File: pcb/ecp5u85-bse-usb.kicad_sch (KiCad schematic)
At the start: 16 parts, among them J1 BSE-040-01-X-D-A, J2 BSE-040-01-X-D-A

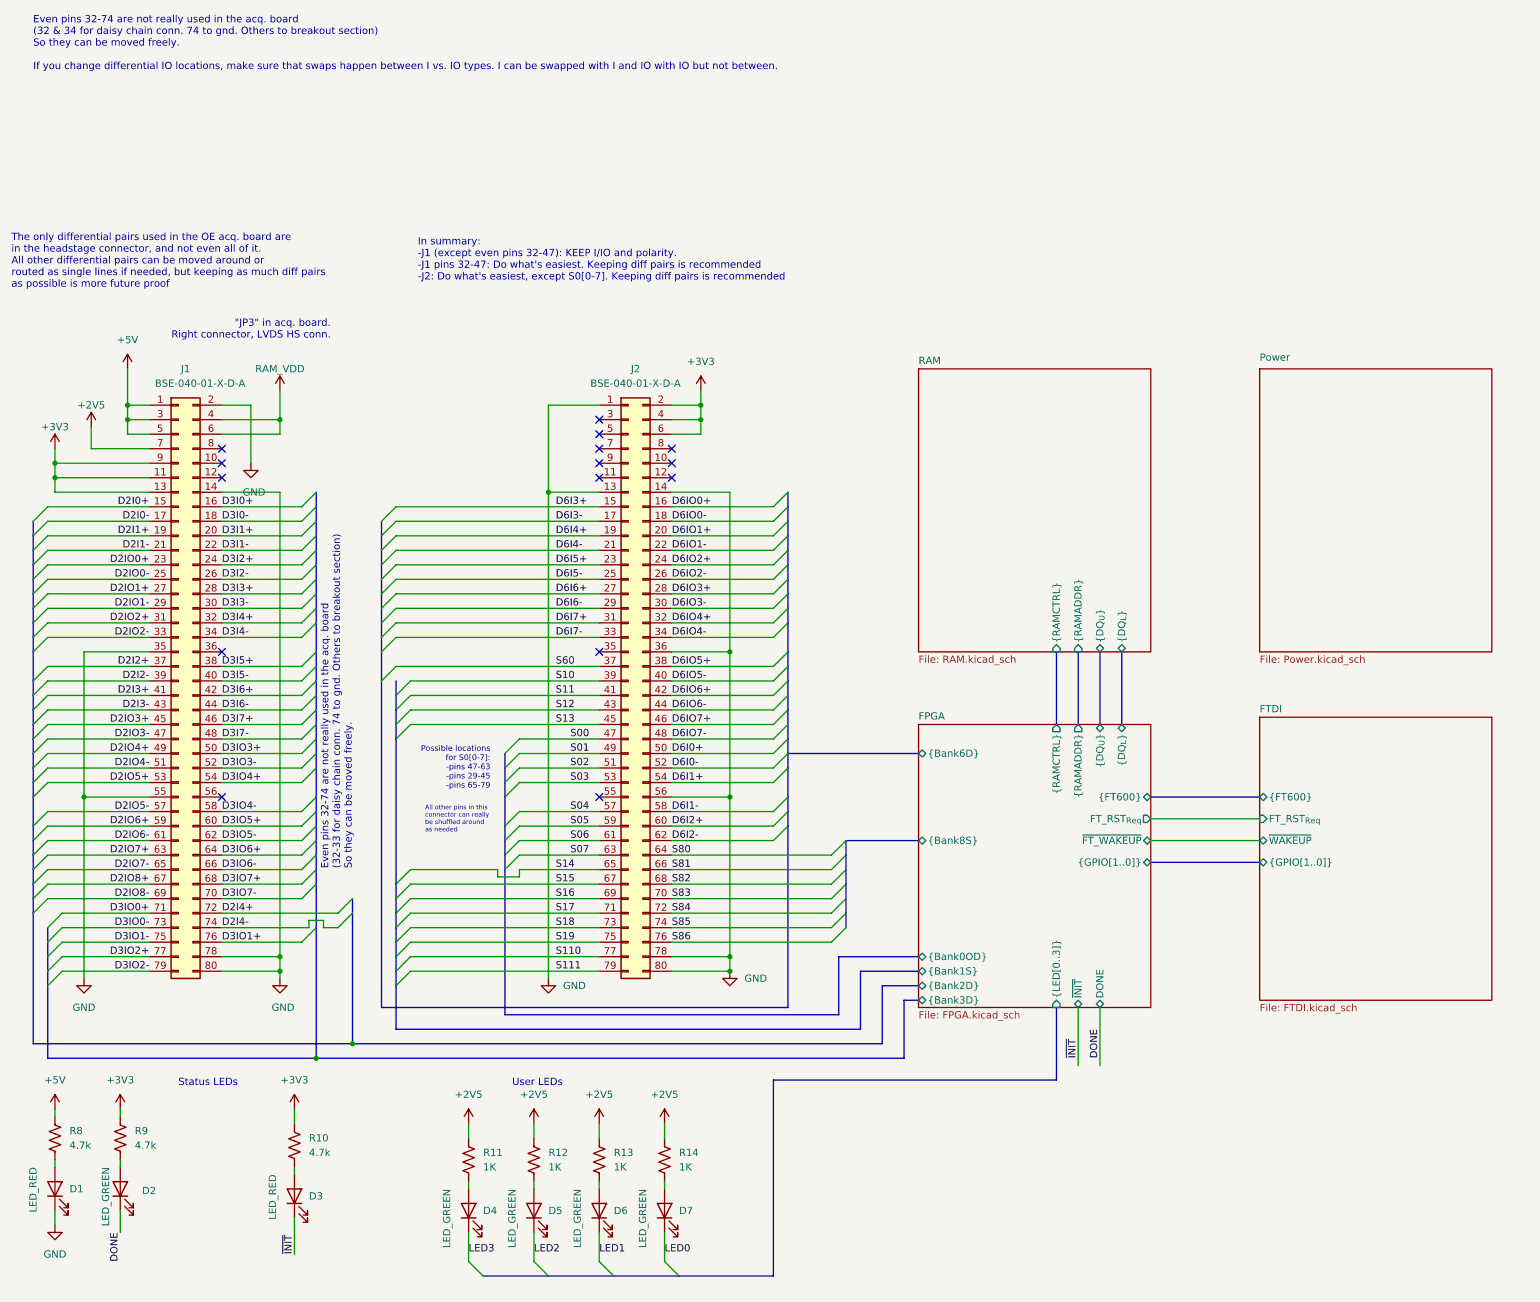
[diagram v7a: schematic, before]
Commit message: Finished IO pin swaping and most of routing
- Left connector is done, includeing trace tuning
- Right conenctor is layed out but needs length tuning
- Decided to move FTDI closer to FPGA and I'm in the middle of that
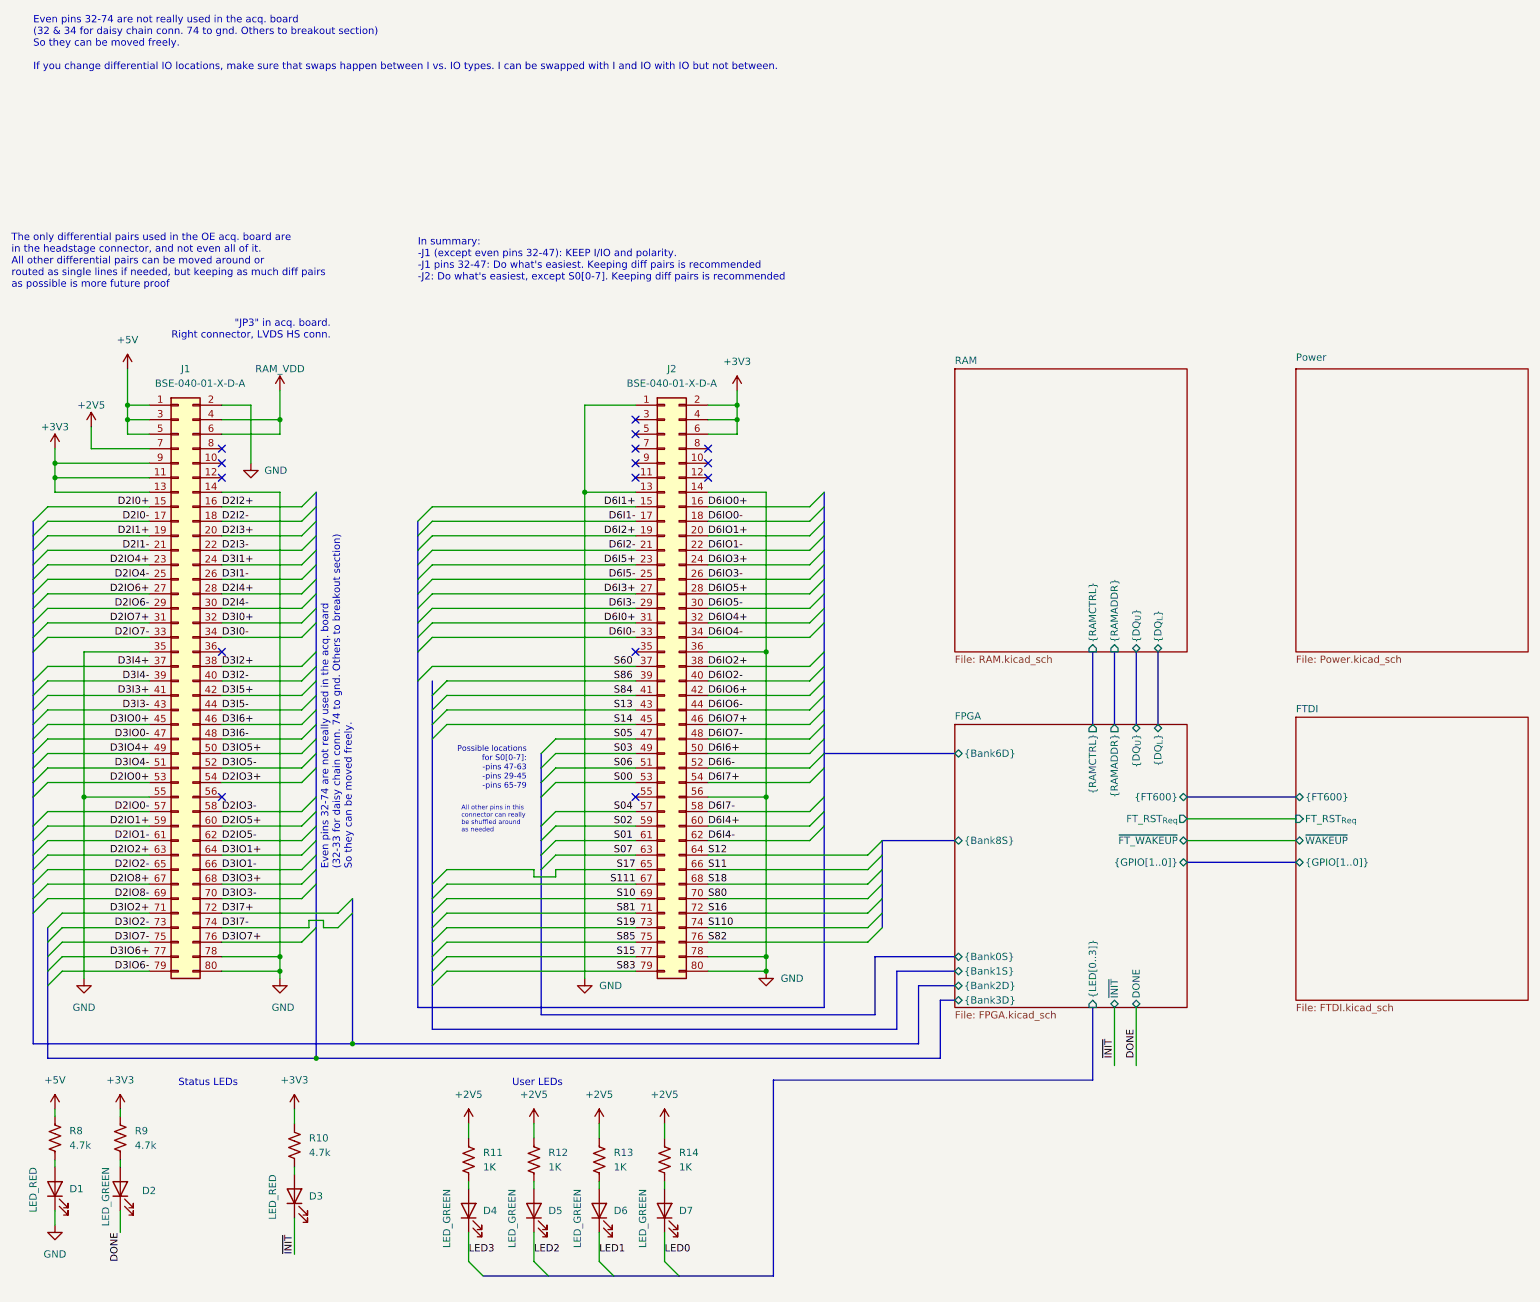
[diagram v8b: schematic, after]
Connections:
- net D2I2+: now also J1.16 (Pin_16); no longer J1.37 (Pin_37)
- net D2I2-: now also J1.18 (Pin_18); no longer J1.39 (Pin_39)
- net D2I3+: now also J1.20 (Pin_20); no longer J1.41 (Pin_41)
- net D2I3-: now also J1.22 (Pin_22); no longer J1.43 (Pin_43)
- net D2I4+: now also J1.28 (Pin_28); no longer J1.72 (Pin_72)
- net D2I4-: now also J1.30 (Pin_30); no longer J1.74 (Pin_74)
- net D2IO0+: now also J1.53 (Pin_53); no longer J1.23 (Pin_23)
- net D2IO0-: now also J1.57 (Pin_57); no longer J1.25 (Pin_25)
- net D2IO1+: now also J1.59 (Pin_59); no longer J1.27 (Pin_27)
- net D2IO1-: now also J1.61 (Pin_61); no longer J1.29 (Pin_29)
- net D2IO2+: now also J1.63 (Pin_63); no longer J1.31 (Pin_31)
- net D2IO2-: now also J1.65 (Pin_65); no longer J1.33 (Pin_33)
- net D2IO3+: now also J1.54 (Pin_54); no longer J1.45 (Pin_45)
- net D2IO3-: now also J1.58 (Pin_58); no longer J1.47 (Pin_47)
- net D2IO4+: now also J1.23 (Pin_23); no longer J1.49 (Pin_49)
- net D2IO4-: now also J1.25 (Pin_25); no longer J1.51 (Pin_51)
- net D2IO5+: now also J1.60 (Pin_60); no longer J1.53 (Pin_53)
- net D2IO5-: now also J1.62 (Pin_62); no longer J1.57 (Pin_57)
- net D2IO6+: now also J1.27 (Pin_27); no longer J1.59 (Pin_59)
- net D2IO6-: now also J1.29 (Pin_29); no longer J1.61 (Pin_61)
- net D2IO7+: now also J1.31 (Pin_31); no longer J1.63 (Pin_63)
- net D2IO7-: now also J1.33 (Pin_33); no longer J1.65 (Pin_65)
- net D3I0+: now also J1.32 (Pin_32); no longer J1.16 (Pin_16)
- net D3I0-: now also J1.34 (Pin_34); no longer J1.18 (Pin_18)
- net D3I1+: now also J1.24 (Pin_24); no longer J1.20 (Pin_20)
- net D3I1-: now also J1.26 (Pin_26); no longer J1.22 (Pin_22)
- net D3I2+: now also J1.38 (Pin_38); no longer J1.24 (Pin_24)
- net D3I2-: now also J1.40 (Pin_40); no longer J1.26 (Pin_26)
- net D3I3+: now also J1.41 (Pin_41); no longer J1.28 (Pin_28)
- net D3I3-: now also J1.43 (Pin_43); no longer J1.30 (Pin_30)
- net D3I4+: now also J1.37 (Pin_37); no longer J1.32 (Pin_32)
- net D3I4-: now also J1.39 (Pin_39); no longer J1.34 (Pin_34)
- net D3I5+: now also J1.42 (Pin_42); no longer J1.38 (Pin_38)
- net D3I5-: now also J1.44 (Pin_44); no longer J1.40 (Pin_40)
- net D3I6+: now also J1.46 (Pin_46); no longer J1.42 (Pin_42)
- net D3I6-: now also J1.48 (Pin_48); no longer J1.44 (Pin_44)
- net D3I7+: now also J1.72 (Pin_72); no longer J1.46 (Pin_46)
- net D3I7-: now also J1.74 (Pin_74); no longer J1.48 (Pin_48)
- net D3IO0+: now also J1.45 (Pin_45); no longer J1.71 (Pin_71)
- net D3IO0-: now also J1.47 (Pin_47); no longer J1.73 (Pin_73)
- net D3IO1+: now also J1.64 (Pin_64); no longer J1.76 (Pin_76)
- net D3IO1-: now also J1.66 (Pin_66); no longer J1.75 (Pin_75)
- net D3IO2+: now also J1.71 (Pin_71); no longer J1.77 (Pin_77)
- net D3IO2-: now also J1.73 (Pin_73); no longer J1.79 (Pin_79)
- net D3IO3+: now also J1.68 (Pin_68); no longer J1.50 (Pin_50)
- net D3IO3-: now also J1.70 (Pin_70); no longer J1.52 (Pin_52)
- net D3IO4+: now also J1.49 (Pin_49); no longer J1.54 (Pin_54)
- net D3IO4-: now also J1.51 (Pin_51); no longer J1.58 (Pin_58)
- net D3IO5+: now also J1.50 (Pin_50); no longer J1.60 (Pin_60)
- net D3IO5-: now also J1.52 (Pin_52); no longer J1.62 (Pin_62)
- net D3IO6+: now also J1.77 (Pin_77); no longer J1.64 (Pin_64)
- net D3IO6-: now also J1.79 (Pin_79); no longer J1.66 (Pin_66)
- net D3IO7+: now also J1.76 (Pin_76); no longer J1.68 (Pin_68)
- net D3IO7-: now also J1.75 (Pin_75); no longer J1.70 (Pin_70)
- net D6I0+: now also J2.31 (Pin_31); no longer J2.50 (Pin_50)
- net D6I0-: now also J2.33 (Pin_33); no longer J2.52 (Pin_52)
- net D6I1+: now also J2.15 (Pin_15); no longer J2.54 (Pin_54)
- net D6I1-: now also J2.17 (Pin_17); no longer J2.58 (Pin_58)
- net D6I2+: now also J2.19 (Pin_19); no longer J2.60 (Pin_60)
- net D6I2-: now also J2.21 (Pin_21); no longer J2.62 (Pin_62)
- net D6I3+: now also J2.27 (Pin_27); no longer J2.15 (Pin_15)
- net D6I3-: now also J2.29 (Pin_29); no longer J2.17 (Pin_17)
- net D6I4+: now also J2.60 (Pin_60); no longer J2.19 (Pin_19)
- net D6I4-: now also J2.62 (Pin_62); no longer J2.21 (Pin_21)
- net D6I6+: now also J2.50 (Pin_50); no longer J2.27 (Pin_27)
- net D6I6-: now also J2.52 (Pin_52); no longer J2.29 (Pin_29)
- net D6I7+: now also J2.54 (Pin_54); no longer J2.31 (Pin_31)
- net D6I7-: now also J2.58 (Pin_58); no longer J2.33 (Pin_33)
- net D6IO2+: now also J2.38 (Pin_38); no longer J2.24 (Pin_24)
- net D6IO2-: now also J2.40 (Pin_40); no longer J2.26 (Pin_26)
- net D6IO3+: now also J2.24 (Pin_24); no longer J2.28 (Pin_28)
- net D6IO3-: now also J2.26 (Pin_26); no longer J2.30 (Pin_30)
- net D6IO5+: now also J2.28 (Pin_28); no longer J2.38 (Pin_38)
- net D6IO5-: now also J2.30 (Pin_30); no longer J2.40 (Pin_40)
- net S00: now also J2.53 (Pin_53); no longer J2.47 (Pin_47)
- net S01: now also J2.61 (Pin_61); no longer J2.49 (Pin_49)
- net S02: now also J2.59 (Pin_59); no longer J2.51 (Pin_51)
- net S03: now also J2.49 (Pin_49); no longer J2.53 (Pin_53)
- net S05: now also J2.47 (Pin_47); no longer J2.59 (Pin_59)
- net S06: now also J2.51 (Pin_51); no longer J2.61 (Pin_61)
- net S10: now also J2.69 (Pin_69); no longer J2.39 (Pin_39)
- net S11: now also J2.66 (Pin_66); no longer J2.41 (Pin_41)
- net S110: now also J2.74 (Pin_74); no longer J2.77 (Pin_77)
- net S111: now also J2.67 (Pin_67); no longer J2.79 (Pin_79)
- net S12: now also J2.64 (Pin_64); no longer J2.43 (Pin_43)
- net S13: now also J2.43 (Pin_43); no longer J2.45 (Pin_45)
- net S14: now also J2.45 (Pin_45); no longer J2.65 (Pin_65)
- net S15: now also J2.77 (Pin_77); no longer J2.67 (Pin_67)
- net S16: now also J2.72 (Pin_72); no longer J2.69 (Pin_69)
- net S17: now also J2.65 (Pin_65); no longer J2.71 (Pin_71)
- net S18: now also J2.68 (Pin_68); no longer J2.73 (Pin_73)
- net S19: now also J2.73 (Pin_73); no longer J2.75 (Pin_75)
- net S80: now also J2.70 (Pin_70); no longer J2.64 (Pin_64)
- net S81: now also J2.71 (Pin_71); no longer J2.66 (Pin_66)
- net S82: now also J2.76 (Pin_76); no longer J2.68 (Pin_68)
- net S83: now also J2.79 (Pin_79); no longer J2.70 (Pin_70)
- net S84: now also J2.41 (Pin_41); no longer J2.72 (Pin_72)
- net S85: now also J2.75 (Pin_75); no longer J2.74 (Pin_74)
- net S86: now also J2.39 (Pin_39); no longer J2.76 (Pin_76)
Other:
- sheet FPGA ports: added {Bank0S}; removed {Bank0OD}
- moved on the sheet: J2
